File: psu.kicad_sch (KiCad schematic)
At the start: 20 parts, among them U6 LM2593HV-ADJ, U7 LM2575S-5, U8 LM2575S-3.3

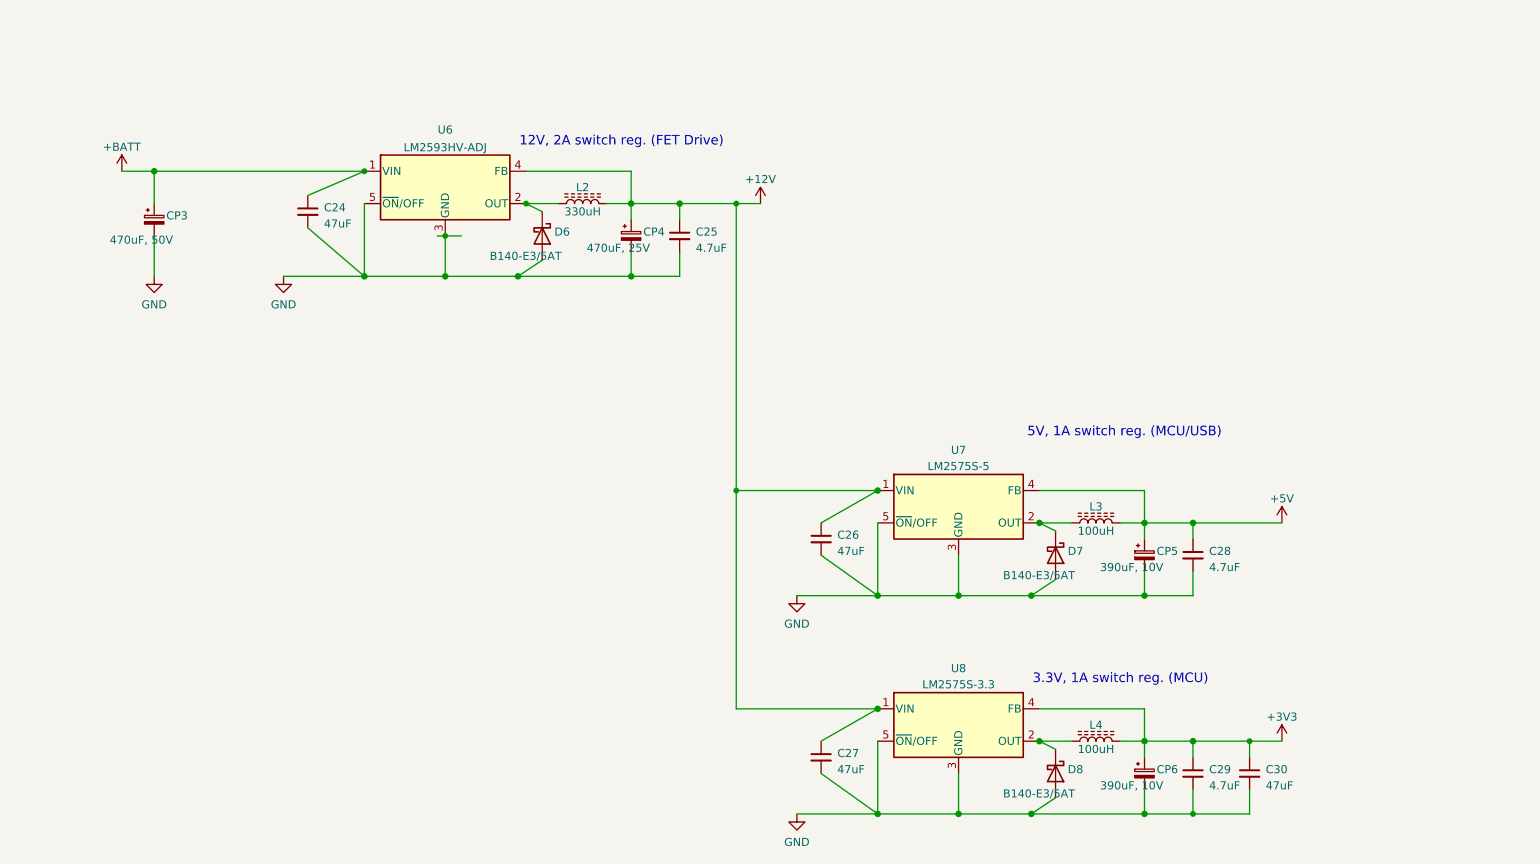
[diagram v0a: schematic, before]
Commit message: Update for Kicad 6-rc; replace 12V reg and cascade; add EEPROM;
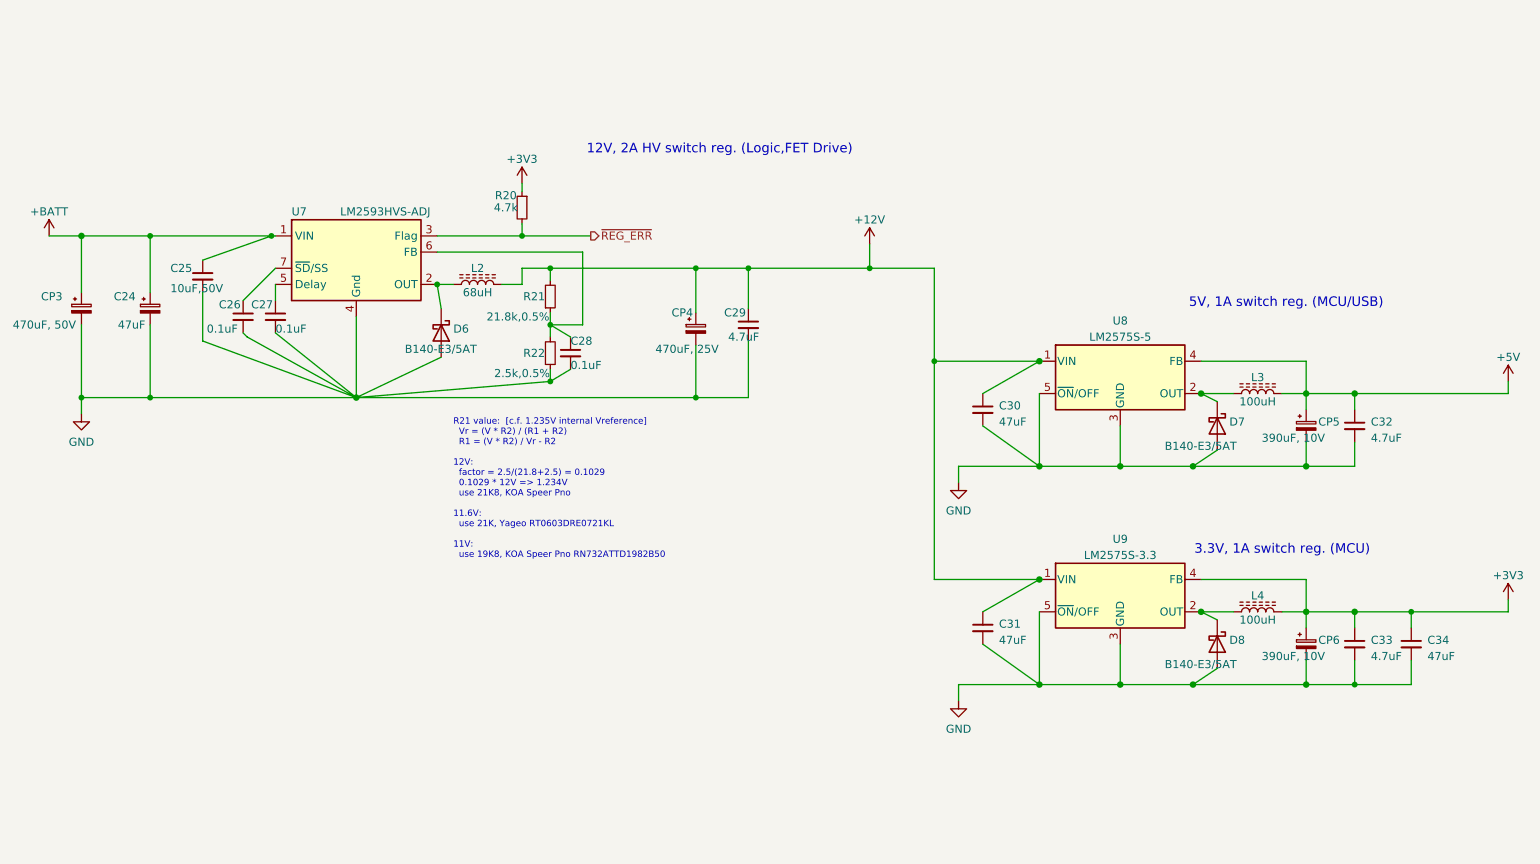
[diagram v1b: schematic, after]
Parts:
- removed U6: LM2593HV-ADJ, solarpump:TO-263-5_TabPin3, symbol Regulator_Switching:LM2576S-5
- added C25: 10uF,50V, Capacitor_SMD:C_0805_2012Metric_Pad1.18x1.45mm_HandSolder, symbol Device:C_Small
- added C26, C27, C28: 0.1uF, Capacitor_SMD:C_0805_2012Metric_Pad1.18x1.45mm_HandSolder, symbol Device:C_Small
- added R20: 4.7k, Resistor_SMD:R_0805_2012Metric_Pad1.20x1.40mm_HandSolder, symbol Device:R_Small
- added R21: 21.8k,0.5%, Resistor_SMD:R_0805_2012Metric_Pad1.20x1.40mm_HandSolder, symbol Device:R_Small
- added R22: 2.5k,0.5%, Resistor_SMD:R_0805_2012Metric_Pad1.20x1.40mm_HandSolder, symbol Device:R_Small
- added U7: LM2593HVS-ADJ, Package_TO_SOT_SMD:TO-263-7_TabPin4, symbol solarpump:LM2593HVS-ADJ
- C24: symbol Device:C_Small -> Device:C_Polarized_Small
- D6: Mfr Part No B140-E3 -> B140-E3/5AT
- L2: value 330uH -> 68uH; footprint Inductor_SMD:L_10.4x10.4_H4.8 -> Inductor_SMD:L_12x12mm_H8mm; Mfr Part No MSS1038-104MLC -> MSS1278H-683KED; Supl Part No 994-MSS1038-104MLC -> 994-MSS1278H-683KED; Supl Price 1.32 -> 2.13
- renumbered C25 to C29, C26 to C30, C27 to C31, C28 to C32, C29 to C33, C30 to C34, U7 to U8, U8 to U9
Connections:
- net +12V: now also R21.2
- net +3V3: now also R20.1
- net +BATT: now also C25.1, U7.1 (VIN)
- net GND: now also C25.2, C26.2, C27.2, C28.2, R22.1, U7.4 (Gnd)
- net at D6.1 (K), L2.1: now also U7.2 (OUT)
- new net: C26.1, U7.7 (~{SD}/SS)
- new net: C28.1, R21.1, R22.2, U7.6 (FB)
- new net: C27.1, U7.5 (Delay)
- new net ~{REG_ERR}: R20.2, U7.3 (Flag)
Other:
- note added: "12V, 2A HV switch reg. (Logic,FET Drive)"
- note added: "R21 value: [c.f. 1.235V internal Vreference] Vr = (V * R2) / (R1 + R2) R1 = (V * R2) / Vr - R2 12V: factor = 2.5/(21.8+2.5) = 0.1029 0.1029 * 12V => 1.234V use 21K8, KOA Speer Pno 11.6V: use 21K, Yageo RT0603DRE0721KL 11V: use 19K8, KOA Speer Pno RN732ATTD1982B50"
- note removed: "12V, 2A switch reg. (FET Drive)"
- moved on the sheet: C29, C30, C31, C32, C33, C34, CP3, CP4, CP5, CP6, D6, D7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

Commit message: Fix diode FP errors, add models; link in regulator error sig; add new coil 3d model; lots of small tweaks
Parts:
- D6, D7, D8: footprint Diode_SMD:D_SOD-123 -> Diode_SMD:D_SMA
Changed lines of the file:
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@@
       (effects (font (size 1.27 1.27)) (justify left))
     )
-    (property "Footprint" "Diode_SMD:D_SOD-123" (id 2) (at 89.535 74.93 0)
+    (property "Footprint" "Diode_SMD:D_SMA" (id 2) (at 89.535 74.93 0)
       (effects (font (size 1.27 1.27)) hide)
     )
@@
       (effects (font (size 1.27 1.27)) (justify left))
     )
-    (property "Footprint" "Diode_SMD:D_SOD-123" (id 2) (at 211.455 89.535 0)
+    (property "Footprint" "Diode_SMD:D_SMA" (id 2) (at 211.455 89.535 0)
       (effects (font (size 1.27 1.27)) hide)
     )
@@
       (effects (font (size 1.27 1.27)) (justify left))
     )
-    (property "Footprint" "Diode_SMD:D_SOD-123" (id 2) (at 211.455 123.825 0)
-      (effects (font (size 1.27 1.27)) hide)
-    )
+    (property "Footprint" "Diode_SMD:D_SMA" (id 2) (at 211.455 123.825 0)
+      (effects (font (size 1.27 1.27)) hide)
+    )

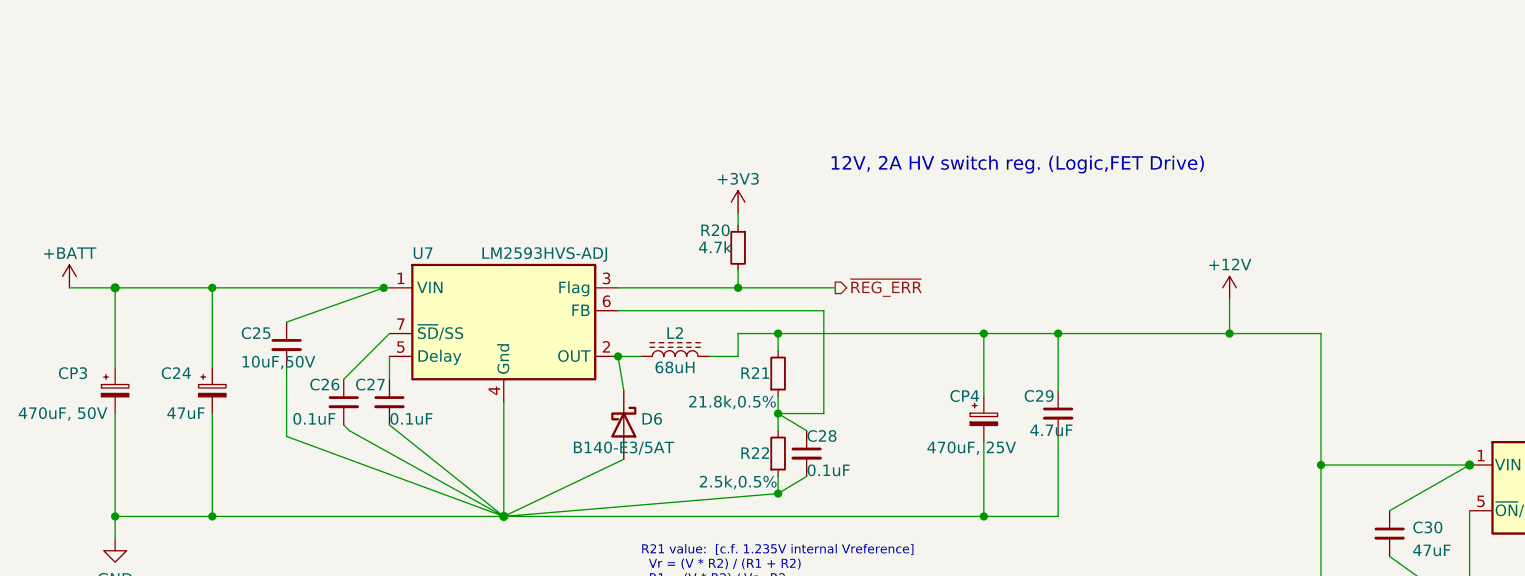
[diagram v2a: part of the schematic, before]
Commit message: Various important tweaks and fixes.
Fix several incorrect capacitor footprints;
Fix slightly incorrect footprint for USB connector;
Add ground vias around MPPT circuit;
Add Zener protection circuit for regulation error input;
Use pin header not socket for Pico Display header;
Fix missing connection to featherwing i2c;
Add in 3d models for USB socket and switch
Update kicad sheet dates;
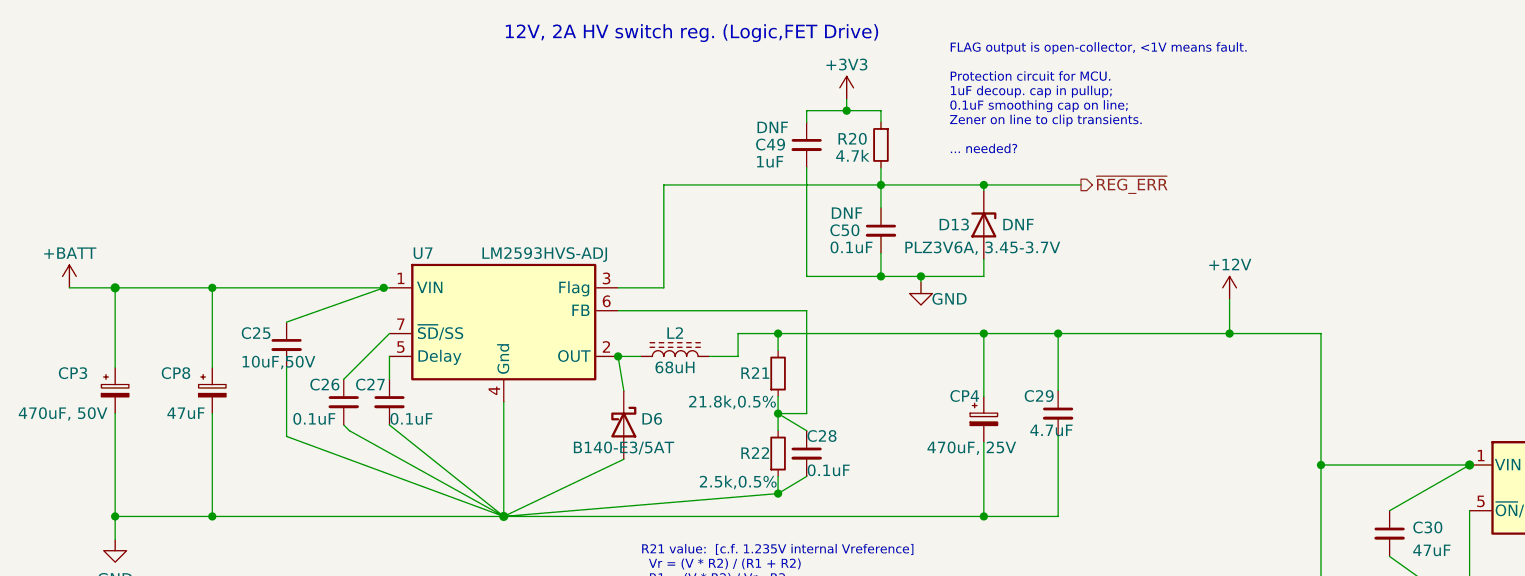
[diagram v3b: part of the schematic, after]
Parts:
- added C49: 1uF, Capacitor_SMD:C_0805_2012Metric_Pad1.18x1.45mm_HandSolder, symbol Device:C_Small
- added C50: 0.1uF, Capacitor_SMD:C_0805_2012Metric_Pad1.18x1.45mm_HandSolder, symbol Device:C_Small
- added D13: PLZ3V6A, 3.45-3.7V, Diode_SMD:D_SMF, symbol Device:D_Zener
- CP3: footprint Capacitor_THT:C_Radial_D12.5mm_H25.0mm_P5.00mm -> Capacitor_THT:CP_Radial_D12.5mm_P5.00mm
- CP4: footprint Capacitor_THT:C_Radial_D10.0mm_H20.0mm_P5.00mm -> Capacitor_THT:CP_Radial_D10.0mm_P5.00mm
- CP5, CP6: footprint Capacitor_THT:C_Radial_D10.0mm_H12.5mm_P5.00mm -> Capacitor_THT:CP_Radial_D8.0mm_P3.50mm
- renumbered C24 to CP8
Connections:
- net +3V3: now also C49.1
- net GND: now also C49.2, C50.2, D13.2 (A)
- net ~{REG_ERR}: now also C50.1, D13.1 (K)
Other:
- note added: "FLAG output is open-collector, <1V means fault. Protection circuit for MCU. 1uF decoup. cap in pullup; 0.1uF smoothing cap on line; Zener on line to clip transients. ... needed?"
- moved on the sheet: R20

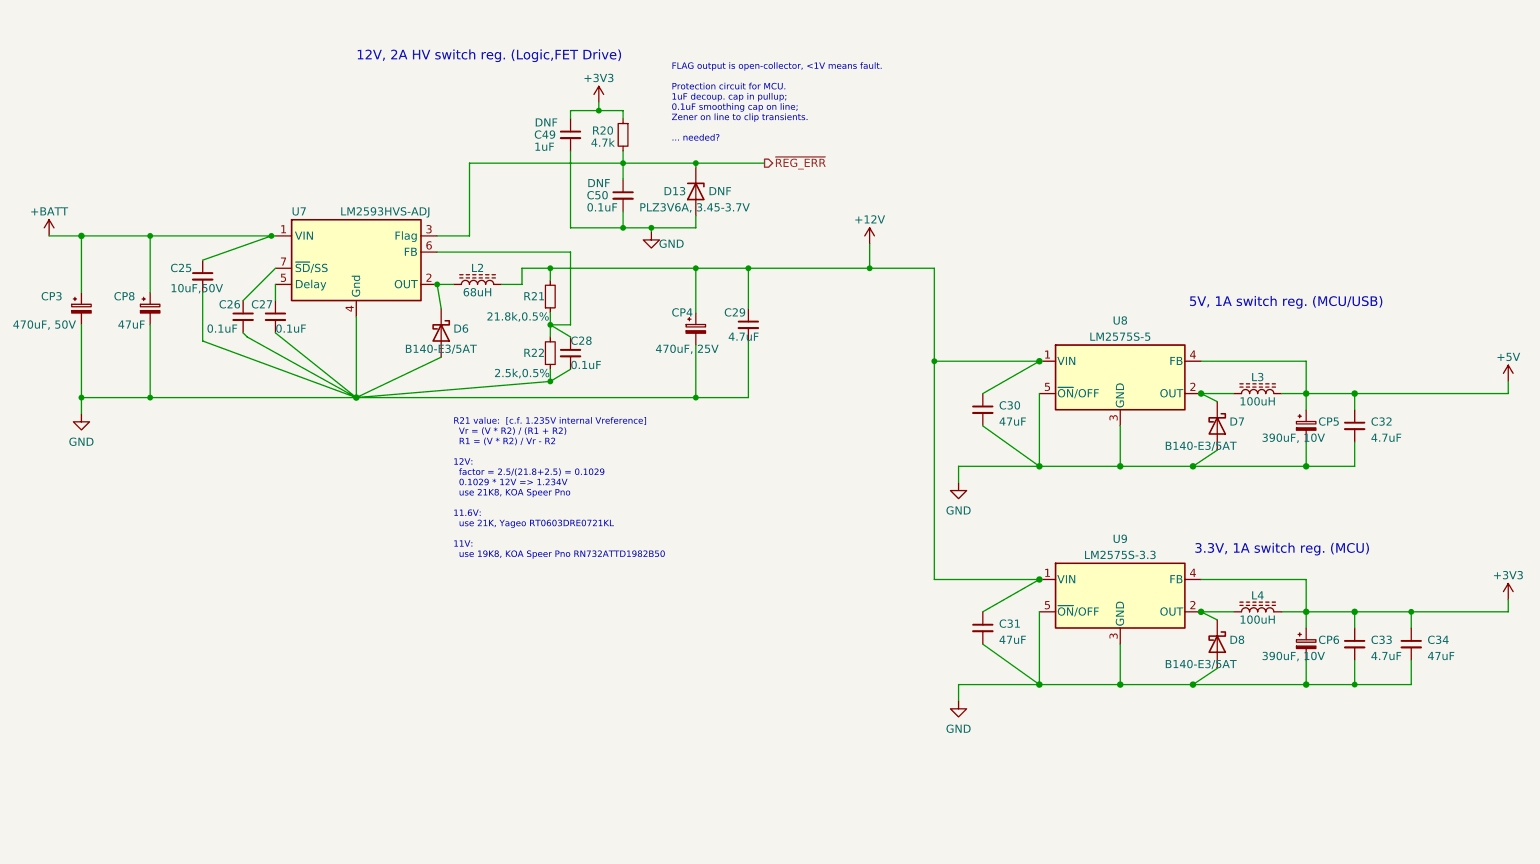
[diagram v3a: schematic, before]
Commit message: Rework with larger display; update component selection; add SWD conn; add RTC chip and QWIIC i2c socket
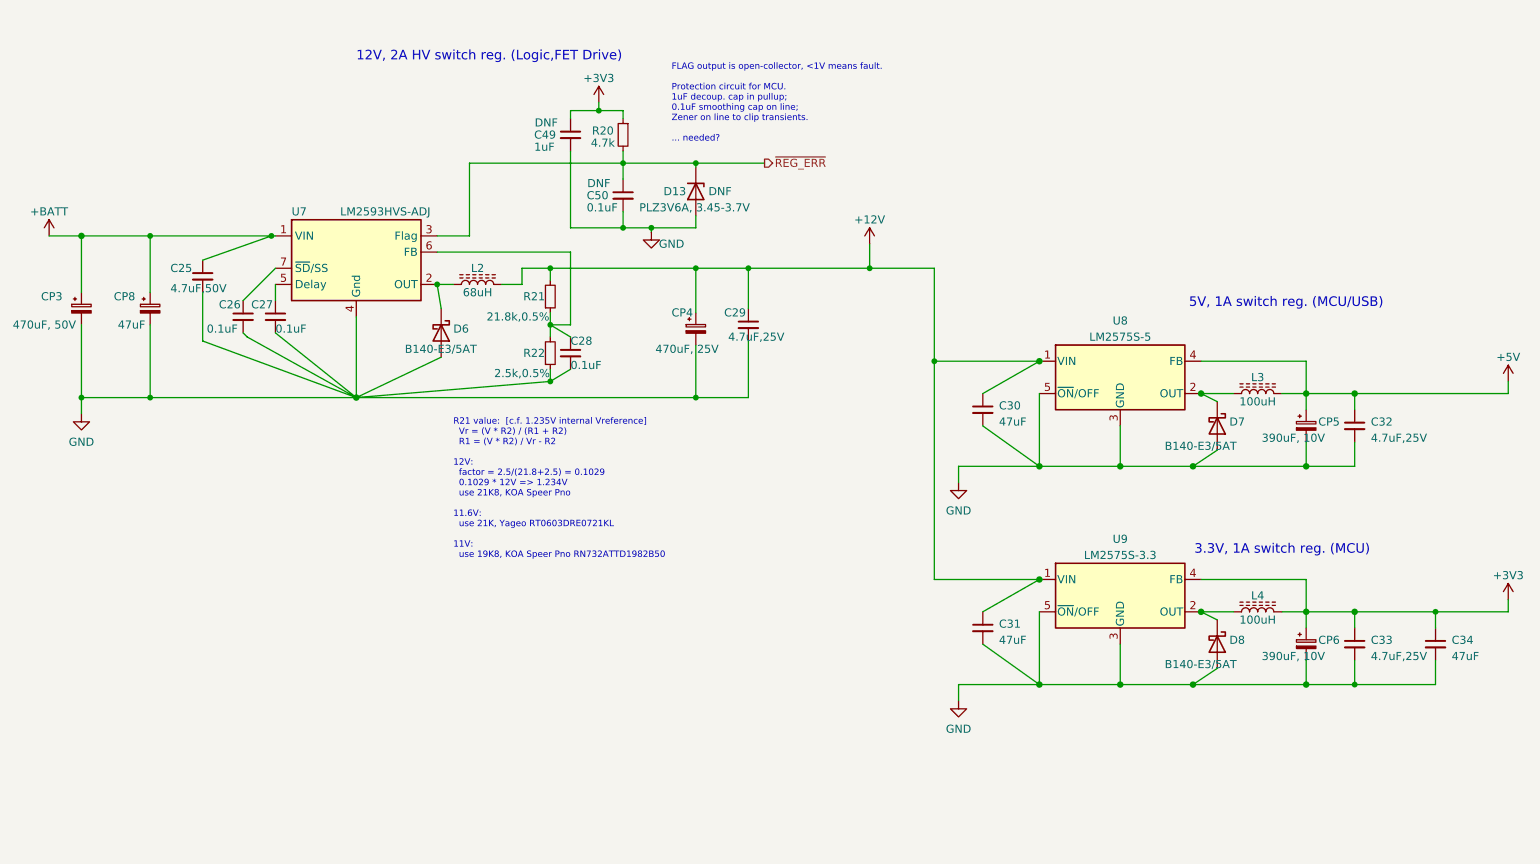
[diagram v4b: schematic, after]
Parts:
- C25: value 10uF,50V -> 4.7uF,50V; Mfr Part No CL31A106MBHNNNE -> CL21A475KBQNNNE; Supl Part No 187-CL31A106MBHNNNE -> 187-CL21A475KBQNNNE; Supl Price 0.254 -> 0.20
- C26, C27, C28: Mfr Name (none) -> C0402C104K8R7411; Mfr Part (none) -> Mouser; Mfr Part No (none) -> CL21B104KACNNND; Part (none) -> 0.016; Price (none) -> KEMET; Repr-Cost (none) -> C0402C104K8R7411; Stock Number (none) -> Mouser; Supl Part No (none) -> 187-CL21B104KACNNND; Supl Price 0.099 -> 0.027
- C29, C32, C33: value 4.7uF -> 4.7uF,25V; Mfr Part No CL21A475KOFNNNG -> CL21A475KAQNNNG; Supl Part No 187-CL21A475KOFNNNG -> 187-CL21A475KAQNNNG; Supl Price 0.099 -> 0.092
- C30, C31: Mfr YAGEO -> CDE / Illinois Capacitor; Mfr Name (none) -> 476KXM050M; Mfr Part (none) -> Mouser; Mfr Part No SK050M047AZS0611 -> 476KXM050M; Part (none) -> 0.269; Price (none) -> CDE / Illinois Capacitor; Repr-Cost (none) -> 476KXM050M; Stock Number (none) -> Mouser; Supl Part No 603-SK050M047AZS0611 -> 598-476KXM050M; Supl Price 0.122 -> 0.269
- C34: Mfr Part No CL31A476MPHNNNE -> 187-CL31A476MQHNNNE; Supl Part No 187-CL31A476MPHNNNE -> 187-CL31A476MQHNNNE; Supl Price 0.38 -> 0.262
- C49: Mfr Samsung Electro-Mechanics -> Taiyo Yuden; Mfr Name (none) -> C0402C104K8R7411; Mfr Part (none) -> Mouser; Mfr Part No CL21A475KOFNNNG -> EMK212BJ105KG-T; Part (none) -> Mouser; Price (none) -> 80-C0402C104K8R7411; Repr-Cost (none) -> 0.016; Stock Number (none) -> C0402C104K8R7411; Supl Part No 187-CL21A475KOFNNNG -> 963-EMK212BJ105KG-T; Supl Price 0.099 -> 0.016
- C50: Mfr Name (none) -> C0402C104K8R7411; Mfr Part (none) -> Mouser; Mfr Part No CL21A475KOFNNNG -> CL21B104KACNNND; Part (none) -> 0.016; Price (none) -> KEMET; Repr-Cost (none) -> C0402C104K8R7411; Stock Number (none) -> Mouser; Supl Part No 187-CL21A475KOFNNNG -> 187-CL21B104KACNNND; Supl Price 0.099 -> 0.027
- D13: Mfr (none) -> Vishay; Mfr Part No (none) -> PLZ3V6A-G3/H; Stock Number 78-PLZ3V6A-G3/H -> (none); Supl (none) -> Mouser; Supl Part No (none) -> 78-PLZ3V6A-G3/H; Supl Price (none) -> 0.23
- U7: Mfr (none) -> TI; Mfr Part No (none) -> LM2593HVSX-ADJ/NOPB; Supl (none) -> Mouser; Supl Part No (none) -> 926-LM2593HVSXADJNPB; Supl Price (none) -> 5.44
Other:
- moved on the sheet: C34
